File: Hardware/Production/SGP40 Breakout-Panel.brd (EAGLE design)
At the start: 175 x 169.2 mm, 1518 parts, among them J10 QWIIC_RIGHT_ANGLE, J100 QWIIC_RIGHT_ANGLE, J101 QWIIC_RIGHT_ANGLE, J103 QWIIC_RIGHT_ANGLE, J104 QWIIC_RIGHT_ANGLE, J106 QWIIC_RIGHT_ANGLE, J107 QWIIC_RIGHT_ANGLE, J11 QWIIC_RIGHT_ANGLE, J13 QWIIC_RIGHT_ANGLE, J14 QWIIC_RIGHT_ANGLE, J16 QWIIC_RIGHT_ANGLE, J17 QWIIC_RIGHT_ANGLE, J19 QWIIC_RIGHT_ANGLE, J2 QWIIC_RIGHT_ANGLE, J20 QWIIC_RIGHT_ANGLE, J22 QWIIC_RIGHT_ANGLE, J23 QWIIC_RIGHT_ANGLE, J25 QWIIC_RIGHT_ANGLE, J26 QWIIC_RIGHT_ANGLE, J28 QWIIC_RIGHT_ANGLE, J29 QWIIC_RIGHT_ANGLE, J3 QWIIC_RIGHT_ANGLE, J31 QWIIC_RIGHT_ANGLE, J32 QWIIC_RIGHT_ANGLE, J34 QWIIC_RIGHT_ANGLE, J35 QWIIC_RIGHT_ANGLE, J37 QWIIC_RIGHT_ANGLE, J38 QWIIC_RIGHT_ANGLE, J4 QWIIC_RIGHT_ANGLE, J40 QWIIC_RIGHT_ANGLE, J41 QWIIC_RIGHT_ANGLE, J43 QWIIC_RIGHT_ANGLE, J44 QWIIC_RIGHT_ANGLE, J46 QWIIC_RIGHT_ANGLE, J47 QWIIC_RIGHT_ANGLE, J49 QWIIC_RIGHT_ANGLE, J5 QWIIC_RIGHT_ANGLE, J50 QWIIC_RIGHT_ANGLE, J52 QWIIC_RIGHT_ANGLE, J53 QWIIC_RIGHT_ANGLE, J55 QWIIC_RIGHT_ANGLE, J56 QWIIC_RIGHT_ANGLE, J58 QWIIC_RIGHT_ANGLE, J59 QWIIC_RIGHT_ANGLE, J61 QWIIC_RIGHT_ANGLE, J62 QWIIC_RIGHT_ANGLE, J64 QWIIC_RIGHT_ANGLE, J65 QWIIC_RIGHT_ANGLE, J67 QWIIC_RIGHT_ANGLE, J68 QWIIC_RIGHT_ANGLE, J7 QWIIC_RIGHT_ANGLE, J70 QWIIC_RIGHT_ANGLE, J71 QWIIC_RIGHT_ANGLE, J73 QWIIC_RIGHT_ANGLE, J74 QWIIC_RIGHT_ANGLE, J76 QWIIC_RIGHT_ANGLE, J77 QWIIC_RIGHT_ANGLE, J79 QWIIC_RIGHT_ANGLE, J8 QWIIC_RIGHT_ANGLE, J80 QWIIC_RIGHT_ANGLE, J82 QWIIC_RIGHT_ANGLE, J83 QWIIC_RIGHT_ANGLE, J85 QWIIC_RIGHT_ANGLE, J86 QWIIC_RIGHT_ANGLE, J88 QWIIC_RIGHT_ANGLE, J89 QWIIC_RIGHT_ANGLE, J91 QWIIC_RIGHT_ANGLE, J92 QWIIC_RIGHT_ANGLE, J94 QWIIC_RIGHT_ANGLE, J95 QWIIC_RIGHT_ANGLE, J97 QWIIC_RIGHT_ANGLE, J98 QWIIC_RIGHT_ANGLE, U1 SGP40, U10 SGP40, U11 SGP40, U12 SGP40, U13 SGP40, U14 SGP40, U15 SGP40, U16 SGP40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

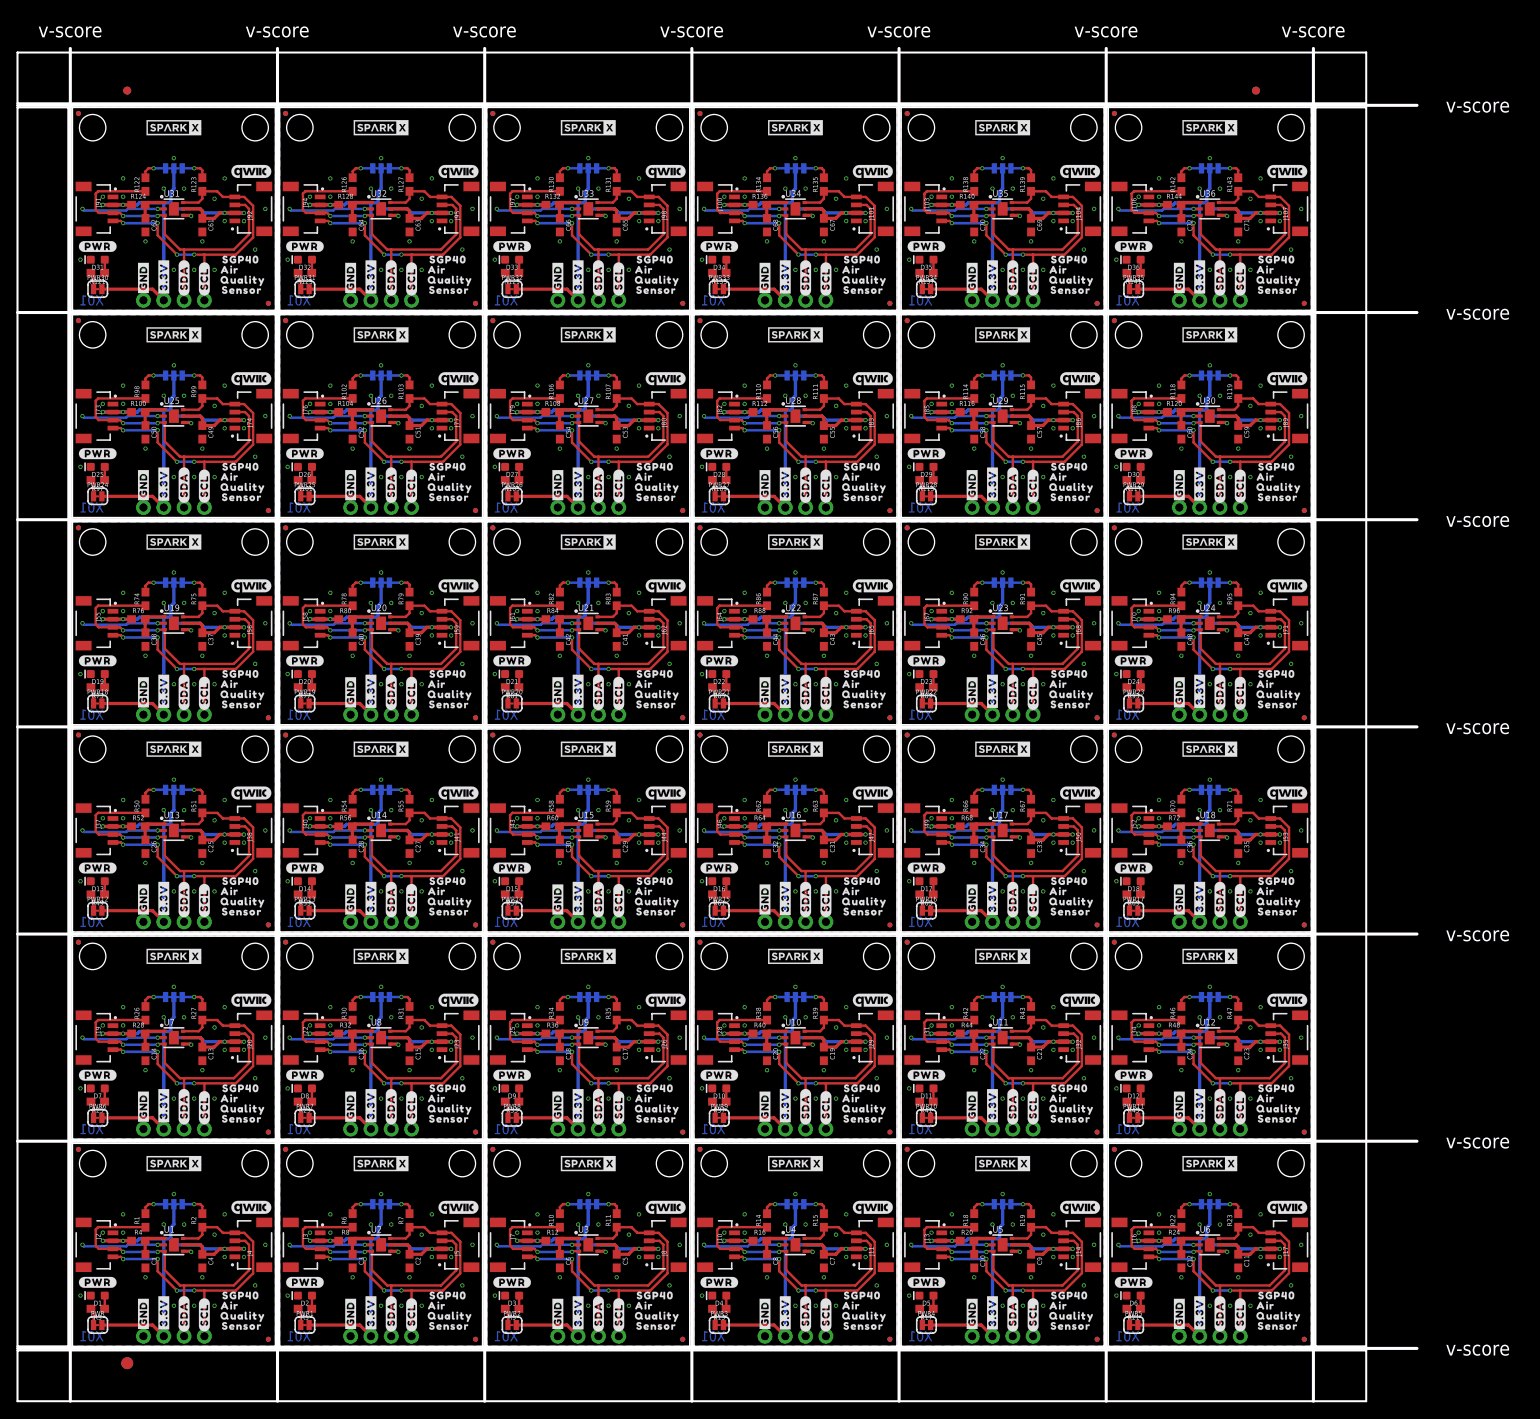
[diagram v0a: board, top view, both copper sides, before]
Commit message: Remove New-Parts. Tweak 0.3mm drill size.
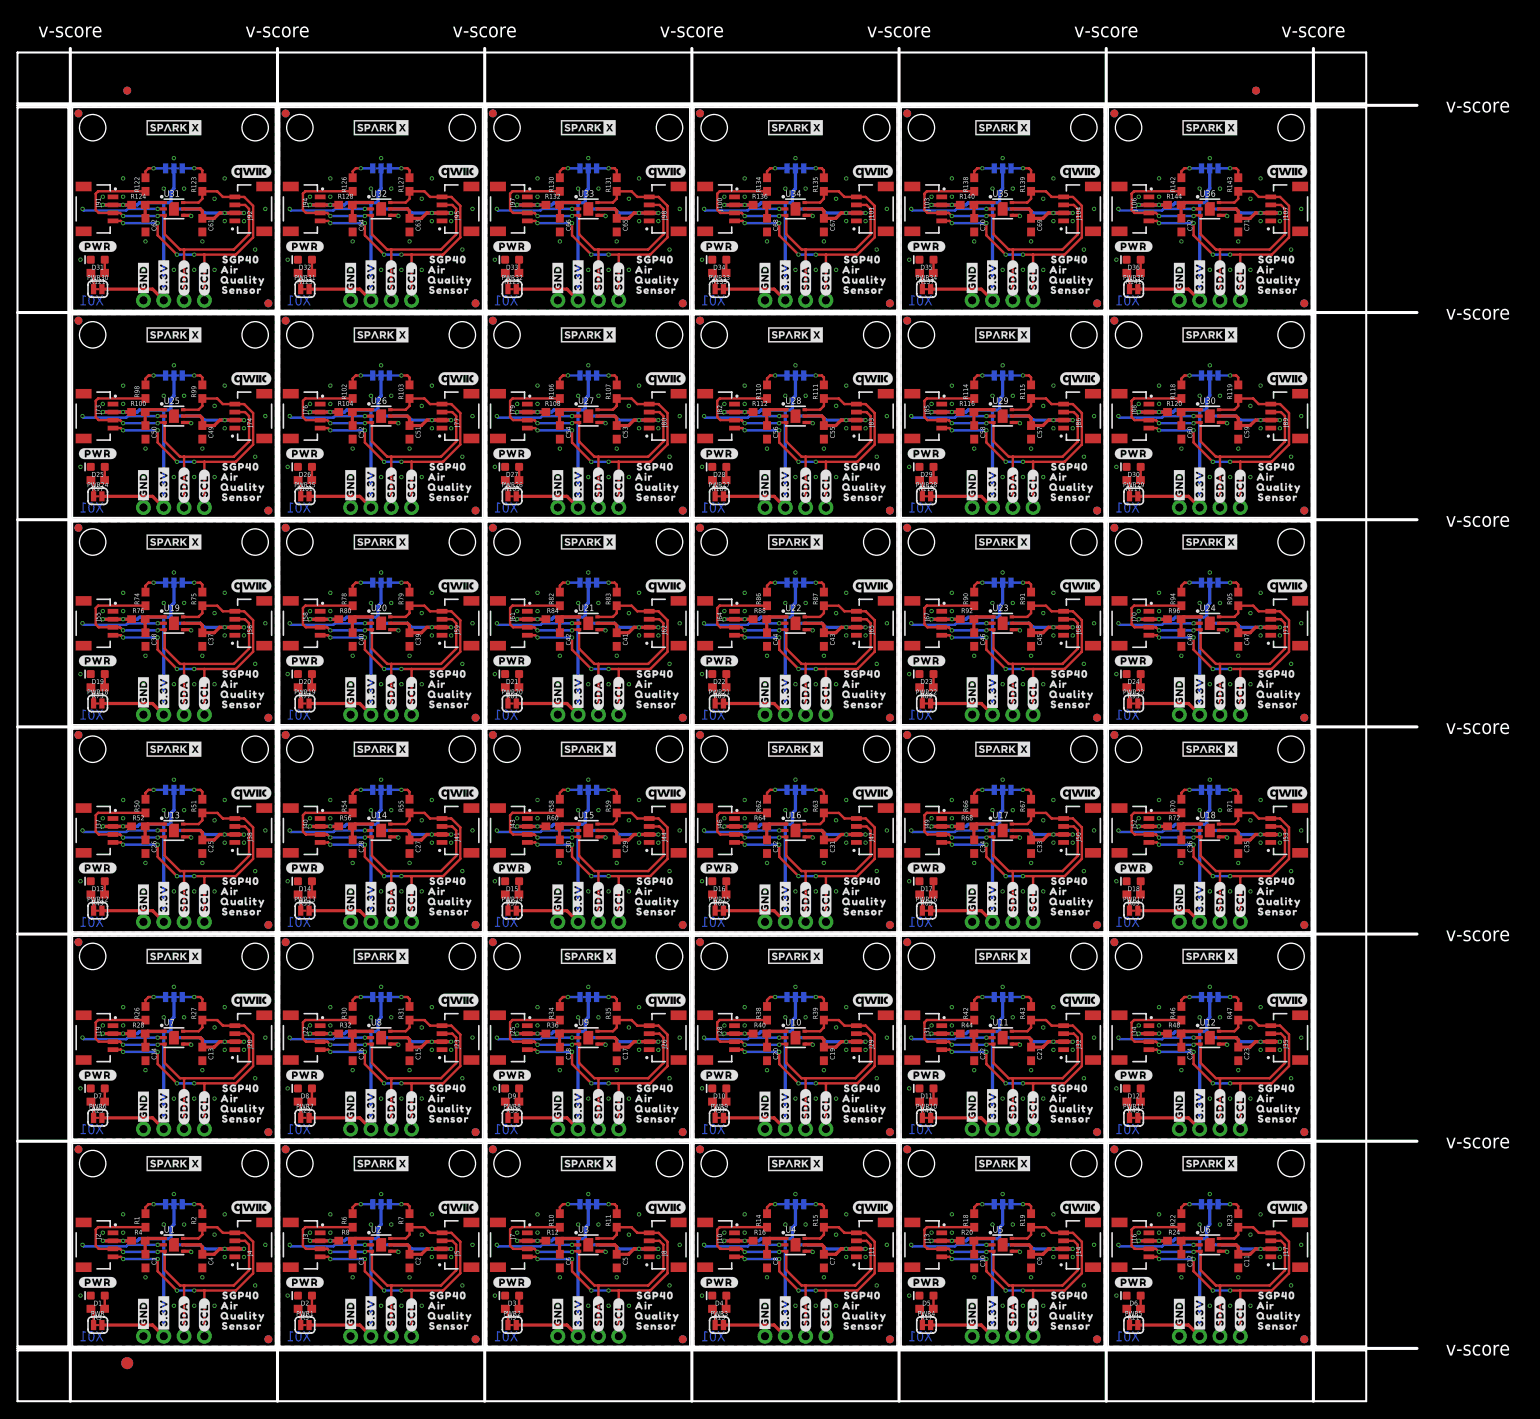
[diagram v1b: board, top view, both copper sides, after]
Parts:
- JP1, JP10, JP100, JP101, JP102, JP105, JP106, JP107, JP108, JP11, JP111, JP112, JP113, JP114, JP117, JP118, JP119, JP12, JP120, JP123, JP124, JP125, JP126, JP129, JP130, JP131, JP132, JP135, JP136, JP137, JP138, JP141, JP142, JP143, JP144, JP147, JP148, JP149, JP15, JP150, JP153, JP154, JP155, JP156, JP159, JP16, JP160, JP161, JP162, JP165, JP166, JP167, JP168, JP17, JP171, JP172, JP173, JP174, JP177, JP178, JP179, JP18, JP180, JP183, JP184, JP185, JP186, JP189, JP190, JP191, JP192, JP195, JP196, JP197, JP198, JP2, JP201, JP202, JP203, JP204, JP207, JP208, JP209, JP21, JP210, JP213, JP214, JP215, JP216, JP22, JP23, JP24, JP27, JP28, JP29, JP30, JP33, JP34, JP35, JP36, JP39, JP40, JP41, JP42, JP45, JP46, JP47, JP48, JP5, JP51, JP52, JP53, JP54, JP57, JP58, JP59, JP6, JP60, JP63, JP64, JP65, JP66, JP69, JP70, JP71, JP72, JP75, JP76, JP77, JP78, JP81, JP82, JP83, JP84, JP87, JP88, JP89, JP9, JP90, JP93, JP94, JP95, JP96, JP99: value FIDUCIALUFIDUCIAL -> FIDUCIAL1X2; device SparkFun:MICRO-FIDUCIAL -> SparkFun-Aesthetics:FIDUCIAL-1X2
- JP103, JP104, JP109, JP110, JP115, JP116, JP121, JP122, JP127, JP128, JP13, JP133, JP134, JP139, JP14, JP140, JP145, JP146, JP151, JP152, JP157, JP158, JP163, JP164, JP169, JP170, JP175, JP176, JP181, JP182, JP187, JP188, JP19, JP193, JP194, JP199, JP20, JP200, JP205, JP206, JP211, JP212, JP25, JP26, JP3, JP31, JP32, JP37, JP38, JP4, JP43, JP44, JP49, JP50, JP55, JP56, JP61, JP62, JP67, JP68, JP7, JP73, JP74, JP79, JP8, JP80, JP85, JP86, JP91, JP92, JP97, JP98: device SparkFun:STAND-OFF -> SparkFun-Hardware:STAND-OFF
- R100, R104, R108, R112, R116, R12, R120, R124, R128, R132, R136, R140, R144, R16, R20, R24, R28, R32, R36, R4, R40, R44, R48, R52, R56, R60, R64, R68, R72, R76, R8, R80, R84, R88, R92, R96: device New-Parts_SparkFun-Resistors:0603 -> SparkFun-Resistors:0603
- U1, U10, U11, U12, U13, U14, U15, U16, U17, U18, U19, U2, U20, U21, U22, U23, U24, U25, U26, U27, U28, U29, U3, U30, U31, U32, U33, U34, U35, U36, U4, U5, U6, U7, U8, U9: device New-Parts_SparkFun-Sensors:SGP40 -> SparkFun-Sensors:SGP40
